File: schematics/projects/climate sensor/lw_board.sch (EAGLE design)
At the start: 34 parts, among them J10 J2, J12 J4_FS_2, J5 KF301-5.0, J6 KF301-5.0, Q1 2N3904, Q2 2N3904, Q3 2N3904, Q4 2N3904, Q5 2N3904, Q6 2N3904, U1 GY-SGP30, U2 ESP32 DEVKIT WROOM-32D, U3 PMS7003, U4 BH1750, U5 BME280, U6 MH_Z19B

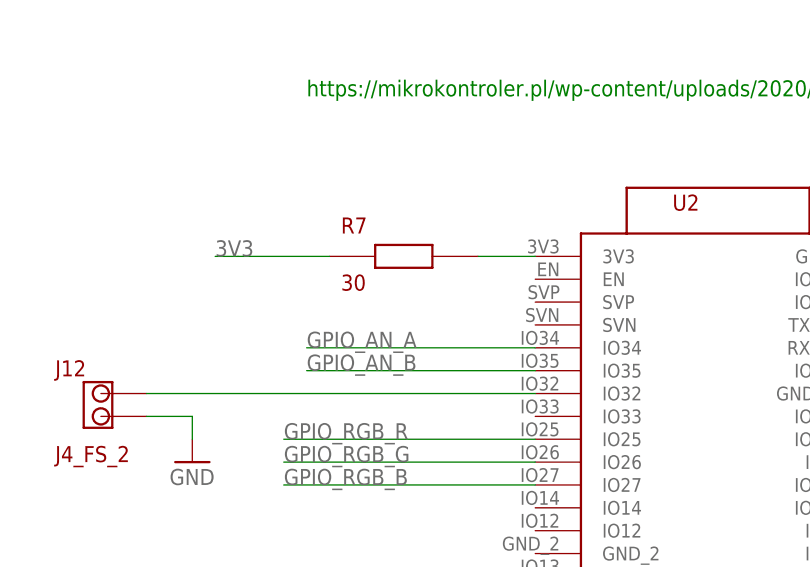
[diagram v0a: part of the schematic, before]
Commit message: SGP30 sensor works now. I2C bus fully tested.
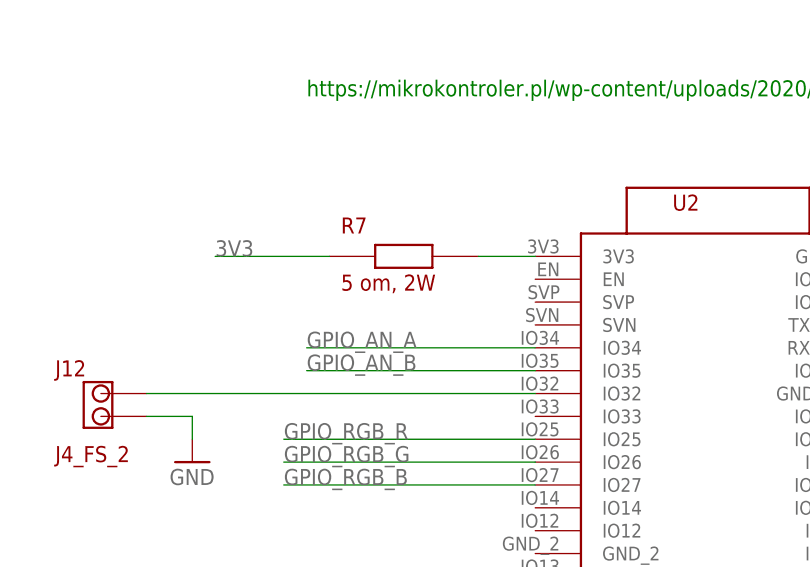
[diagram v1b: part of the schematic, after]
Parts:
- R7: value 30 -> 5 om, 2W
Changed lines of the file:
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@@
 <part name="GND1" library="supply1" library_urn="urn:adsk.eagle:library:371" deviceset="GND" device=""/>
 <part name="GND9" library="supply1" library_urn="urn:adsk.eagle:library:371" deviceset="GND" device=""/>
-<part name="R7" library="my_devices" deviceset="R" device="" value="30"/>
+<part name="R7" library="my_devices" deviceset="R" device="" value="5 om, 2W"/>
 <part name="J12" library="my_devices" deviceset="J2" device="" value="J4_FS_2"/>
 <part name="U2" library="my_devices" deviceset="ESP32" device="" value="ESP32 DEVKIT WROOM-32D"/>
